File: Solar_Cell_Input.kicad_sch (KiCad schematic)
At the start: 35 parts, among them Q201 BSS138L, Q202 NVTFWS4D9N04XMTAG, Q203 NVTFWS4D9N04XMTAG, U201 BQ24650

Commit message: nearly finnished CORE pcb
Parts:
- renumbered C202 to C201, C204 to C202, C205 to C203, C206 to C204, C207 to C205, C208 to C206, C209 to C207, C210 to C208, C211 to C209, C201 to C210, C203 to C911, R204 to R203, R205 to R204, R206 to R205, R207 to R206, R208 to R207, R209 to R208, R210 to R209, R211 to R210, R212 to R211, R213 to R212, R203 to R913
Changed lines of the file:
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@@
 		(dnp no)
 		(fields_autoplaced yes)
-		(property "Reference" "R211"
+		(property "Reference" "R210"
 			(at 203.2 55.88 90)
 			(effects
@@
 		(dnp no)
 		(fields_autoplaced yes)
-		(property "Reference" "R208"
+		(property "Reference" "R207"
 			(at 139.7 41.9099 0)
 			(effects
@@
 		(on_board yes)
 		(dnp no)
-		(property "Reference" "R210"
+		(property "Reference" "R209"
 			(at 180.594 90.17 0)
 			(effects
@@
 		(on_board yes)
 		(dnp no)
-		(property "Reference" "#PWR0216"
+		(property "Reference" "#PWR0215"
 			(at 213.36 74.93 0)
 			(effects
@@
 		(dnp no)
 		(fields_autoplaced yes)
-		(property "Reference" "#PWR0207"
+		(property "Reference" "#PWR0917"
 			(at 121.92 110.49 0)
 			(effects
@@
 		(on_board yes)
 		(dnp no)
-		(property "Reference" "C207"
+		(property "Reference" "C205"
 			(at 166.878 57.912 90)
 			(effects
@@
 		(on_board yes)
 		(dnp no)
-		(property "Reference" "#PWR0214"
+		(property "Reference" "#PWR0213"
 			(at 189.23 52.07 0)
 			(effects
@@
 		(dnp no)
 		(fields_autoplaced yes)
-		(property "Reference" "R205"
+		(property "Reference" "R204"
 			(at 100.33 78.7399 0)
 			(effects
@@
 		(dnp no)
 		(fields_autoplaced yes)
-		(property "Reference" "R204"
+		(property "Reference" "R203"
 			(at 100.33 66.0399 0)
 			(effects
@@
 		(dnp no)
 		(fields_autoplaced yes)
-		(property "Reference" "#PWR0209"
+		(property "Reference" "#PWR0208"
 			(at 137.16 102.87 0)
 			(effects
@@
 		(on_board yes)
 		(dnp no)
-		(property "Reference" "#PWR0208"
+		(property "Reference" "#PWR0207"
 			(at 123.19 59.69 0)
 			(effects
@@
 		(on_board yes)
 		(dnp no)
-		(property "Reference" "C210"
+		(property "Reference" "C208"
 			(at 208.28 82.5562 0)
 			(effects
@@
 		(on_board yes)
 		(dnp no)
-		(property "Reference" "Q201"
+		(property "Reference" "Q?"
 			(at 91.44 110.49 0)
 			(effects
@@
 				)
 			)
+			(project "EPS"
+				(path "/94201994-47b8-4213-8d1a-05da12b2a7b0/c37f0a0b-f6f4-4c63-8ce8-6ee6766e791f/41c5534f-fcb2-4ec3-adc7-992b7bee1600"
+					(reference "Q?")
+					(unit 1)
+				)
+				(path "/94201994-47b8-4213-8d1a-05da12b2a7b0/c37f0a0b-f6f4-4c63-8ce8-6ee6766e791f/4313468d-8f4f-4bdc-8385-889814f4cee5"
+					(reference "Q?")
+					(unit 1)
+				)
+				(path "/94201994-47b8-4213-8d1a-05da12b2a7b0/c37f0a0b-f6f4-4c63-8ce8-6ee6766e791f/52873e6b-e08e-4161-9ef2-2b4737346b9b"
+					(reference "Q?")
+					(unit 1)
+				)
+				(path "/94201994-47b8-4213-8d1a-05da12b2a7b0/c37f0a0b-f6f4-4c63-8ce8-6ee6766e791f/65753da0-d365-4e1b-a747-1fe94f193180"
+					(reference "Q?")
+					(unit 1)
+				)
+				(path "/94201994-47b8-4213-8d1a-05da12b2a7b0/c37f0a0b-f6f4-4c63-8ce8-6ee6766e791f/6d13a628-cc69-4882-8d71-6117aca3a662"
+					(reference "Q?")
+					(unit 1)
+				)
+				(path "/94201994-47b8-4213-8d1a-05da12b2a7b0/c37f0a0b-f6f4-4c63-8ce8-6ee6766e791f/9d09256a-b1cf-431e-ac15-ed14acab8c88"
+					(reference "Q?")
+					(unit 1)
+				)
+			)
 		)
 	)
@@
 		(dnp no)
 		(fields_autoplaced yes)
-		(property "Reference" "R206"
+		(property "Reference" "R205"
 			(at 107.95 53.3399 0)
 			(effects
@@
 		(on_board yes)
 		(dnp no)
-		(property "Reference" "#PWR0215"
+		(property "Reference" "#PWR0214"
 			(at 208.28 74.93 0)
 			(effects
@@
 		(dnp no)
 		(fields_autoplaced yes)
-		(property "Reference" "R212"
+		(property "Reference" "R211"
 			(at 218.44 82.5499 0)
 			(effects
@@
 		(on_board yes)
 		(dnp no)
-		(property "Reference" "C208"
+		(property "Reference" "C206"
 			(at 191.77 41.9162 0)
 			(effects
@@
 		(on_board yes)
 		(dnp no)
-		(property "Reference" "C209"
+		(property "Reference" "C207"
 			(at 205.74 64.7762 0)
 			(effects
@@
 		(on_board yes)
 		(dnp no)
-		(property "Reference" "#PWR0212"
+		(property "Reference" "#PWR0211"
 			(at 179.07 77.47 0)
 			(effects
@@
 		(on_board yes)
 		(dnp no)
-		(property "Reference" "C204"
+		(property "Reference" "C202"
 			(at 120.65 49.5362 0)
 			(effects
@@
 		(on_board yes)
 		(dnp no)
-		(property "Reference" "C211"
+		(property "Reference" "C209"
 			(at 215.9 64.7762 0)
 			(effects
@@
 		(dnp no)
 		(fields_autoplaced yes)
-		(property "Reference" "#PWR0213"
+		(property "Reference" "#PWR?"
 			(at 173.99 92.71 0)
 			(effects
@@
 				)
 			)
+			(project "EPS"
+				(path "/94201994-47b8-4213-8d1a-05da12b2a7b0/c37f0a0b-f6f4-4c63-8ce8-6ee6766e791f/41c5534f-fcb2-4ec3-adc7-992b7bee1600"
+					(reference "#PWR?")
+					(unit 1)
+				)
+				(path "/94201994-47b8-4213-8d1a-05da12b2a7b0/c37f0a0b-f6f4-4c63-8ce8-6ee6766e791f/4313468d-8f4f-4bdc-8385-889814f4cee5"
+					(reference "#PWR?")
+					(unit 1)
+				)
+				(path "/94201994-47b8-4213-8d1a-05da12b2a7b0/c37f0a0b-f6f4-4c63-8ce8-6ee6766e791f/52873e6b-e08e-4161-9ef2-2b4737346b9b"
+					(reference "#PWR?")
+					(unit 1)
+				)
+				(path "/94201994-47b8-4213-8d1a-05da12b2a7b0/c37f0a0b-f6f4-4c63-8ce8-6ee6766e791f/65753da0-d365-4e1b-a747-1fe94f193180"
+					(reference "#PWR?")
+					(unit 1)
+				)
+				(path "/94201994-47b8-4213-8d1a-05da12b2a7b0/c37f0a0b-f6f4-4c63-8ce8-6ee6766e791f/6d13a628-cc69-4882-8d71-6117aca3a662"
+					(reference "#PWR?")
+					(unit 1)
+				)
+				(path "/94201994-47b8-4213-8d1a-05da12b2a7b0/c37f0a0b-f6f4-4c63-8ce8-6ee6766e791f/9d09256a-b1cf-431e-ac15-ed14acab8c88"
+					(reference "#PWR?")
+					(unit 1)
+				)
+			)
 		)
 	)
@@
 		(on_board yes)
 		(dnp no)
-		(property "Reference" "#PWR0217"
+		(property "Reference" "#PWR0216"
 			(at 215.9 100.33 0)
 			(effects
@@
 		(on_board yes)
 		(dnp no)
-		(property "Reference" "C202"
+		(property "Reference" "C201"
 			(at 113.03 66.0462 0)
 			(effects
@@
 		(dnp no)
 		(fields_autoplaced yes)
-		(property "Reference" "#FLG0201"
+		(property "Reference" "#FLG04701"
 			(at 129.54 45.085 0)
 			(effects
@@
 		(on_board yes)
 		(dnp no)
-		(property "Reference" "C205"
+		(property "Reference" "C203"
 			(at 160.02 72.3962 0)
 			(effects
@@
 		(dnp no)
 		(fields_autoplaced yes)
-		(property "Reference" "#PWR0202"
+		(property "Reference" "#PWR0203"
 			(at 88.9 123.19 0)
 			(effects
@@
 		(on_board yes)
 		(dnp no)
-		(property "Reference" "R209"
+		(property "Reference" "R208"
 			(at 172.212 90.17 0)
 			(effects
@@
 		(dnp no)
 		(fields_autoplaced yes)
-		(property "Reference" "R207"
+		(property "Reference" "R206"
 			(at 107.95 100.3299 0)
 			(effects
@@
 		(on_board yes)
 		(dnp no)
-		(property "Reference" "C203"
+		(property "Reference" "C911"
 			(at 119.38 100.3362 0)
 			(effects
@@
 		(on_board yes)
 		(dnp no)
-		(property "Reference" "#PWR0210"
+		(property "Reference" "#PWR0209"
 			(at 158.75 55.88 0)
 			(effects
@@
 		(dnp no)
 		(fields_autoplaced yes)
-		(property "Reference" "R203"
+		(property "Reference" "R913"
 			(at 91.44 100.3299 0)
 			(effects
@@
 		(on_board yes)
 		(dnp no)
-		(property "Reference" "C201"
+		(property "Reference" "C210"
 			(at 95.25 46.9962 0)
 			(effects
@@
 		(on_board yes)
 		(dnp no)
-		(property "Reference" "#PWR0203"
+		(property "Reference" "#PWR0202"
 			(at 97.79 57.15 0)
 			(effects
@@
 		(dnp no)
 		(fields_autoplaced yes)
-		(property "Reference" "#PWR0211"
+		(property "Reference" "#PWR?"
 			(at 179.07 92.71 0)
 			(effects
@@
 				)
 			)
+			(project "EPS"
+				(path "/94201994-47b8-4213-8d1a-05da12b2a7b0/c37f0a0b-f6f4-4c63-8ce8-6ee6766e791f/41c5534f-fcb2-4ec3-adc7-992b7bee1600"
+					(reference "#PWR?")
+					(unit 1)
+				)
+				(path "/94201994-47b8-4213-8d1a-05da12b2a7b0/c37f0a0b-f6f4-4c63-8ce8-6ee6766e791f/4313468d-8f4f-4bdc-8385-889814f4cee5"
+					(reference "#PWR?")
+					(unit 1)
+				)
+				(path "/94201994-47b8-4213-8d1a-05da12b2a7b0/c37f0a0b-f6f4-4c63-8ce8-6ee6766e791f/52873e6b-e08e-4161-9ef2-2b4737346b9b"
+					(reference "#PWR?")
+					(unit 1)
+				)
+				(path "/94201994-47b8-4213-8d1a-05da12b2a7b0/c37f0a0b-f6f4-4c63-8ce8-6ee6766e791f/65753da0-d365-4e1b-a747-1fe94f193180"
+					(reference "#PWR?")
+					(unit 1)
+				)
+				(path "/94201994-47b8-4213-8d1a-05da12b2a7b0/c37f0a0b-f6f4-4c63-8ce8-6ee6766e791f/6d13a628-cc69-4882-8d71-6117aca3a662"
+					(reference "#PWR?")
+					(unit 1)
+				)
+				(path "/94201994-47b8-4213-8d1a-05da12b2a7b0/c37f0a0b-f6f4-4c63-8ce8-6ee6766e791f/9d09256a-b1cf-431e-ac15-ed14acab8c88"
+					(reference "#PWR?")
+					(unit 1)
+				)
+			)
 		)
 	)
@@
 		(on_board yes)
 		(dnp no)
-		(property "Reference" "C206"
+		(property "Reference" "C204"
 			(at 156.21 45.7262 0)
 			(effects
@@
 		(dnp no)
 		(fields_autoplaced yes)
-		(property "Reference" "R213"
+		(property "Reference" "R212"
 			(at 218.44 90.1699 0)
 			(effects

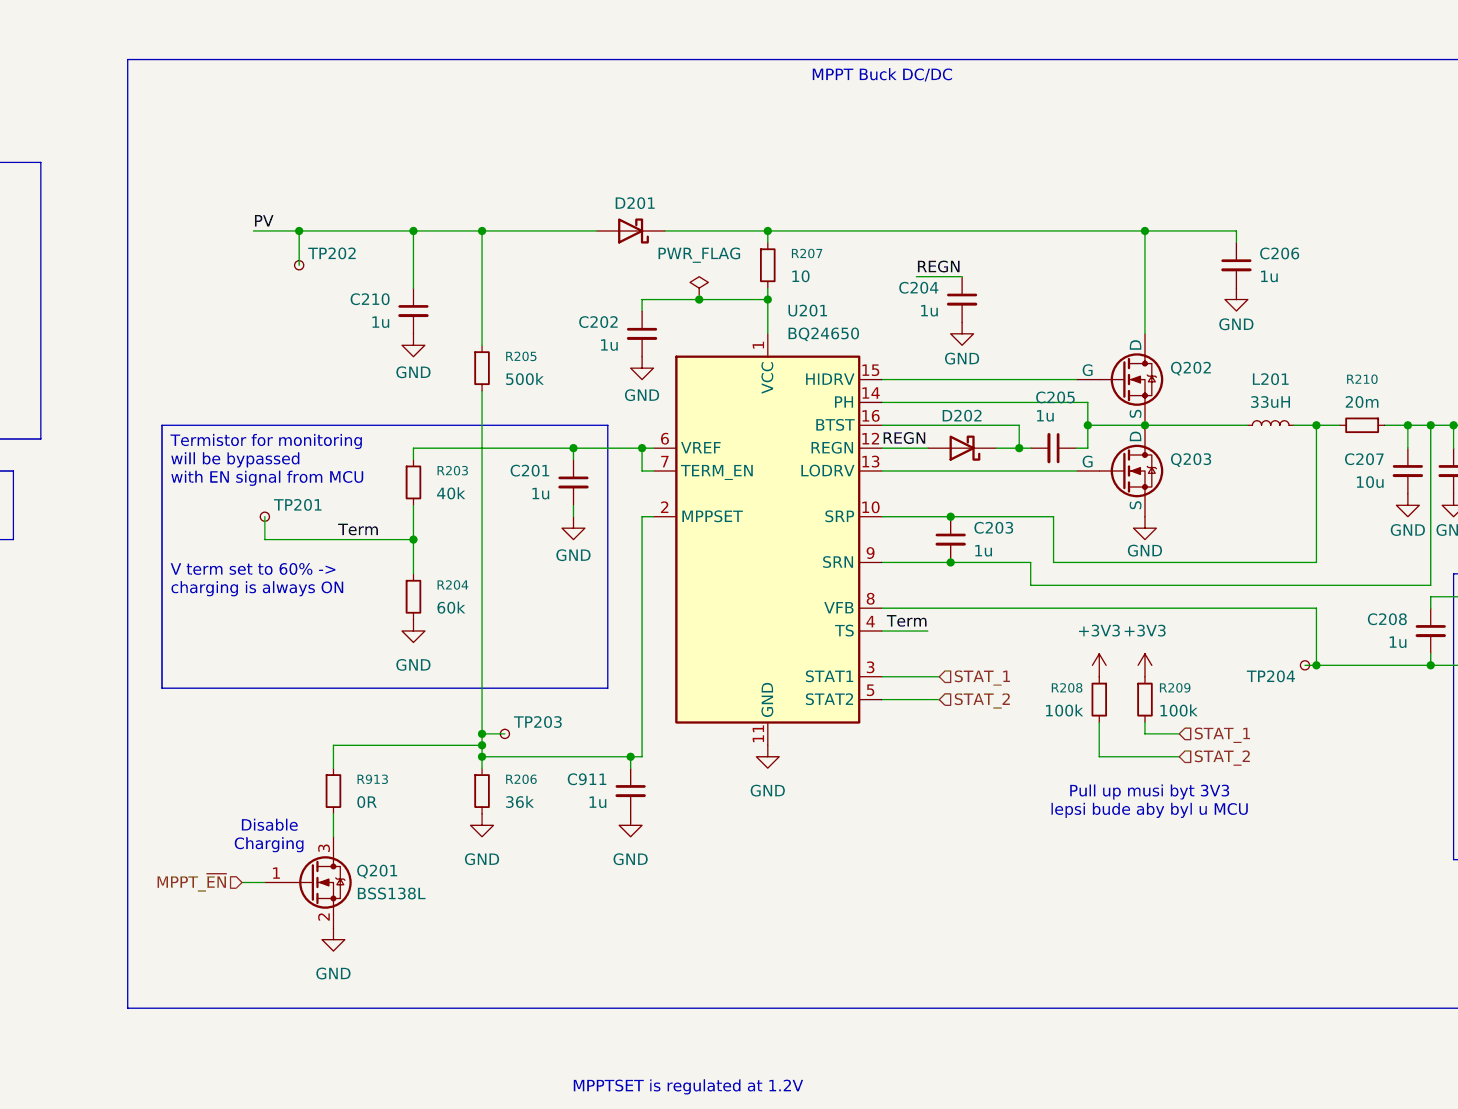
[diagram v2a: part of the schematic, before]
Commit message: pcb progres for all components
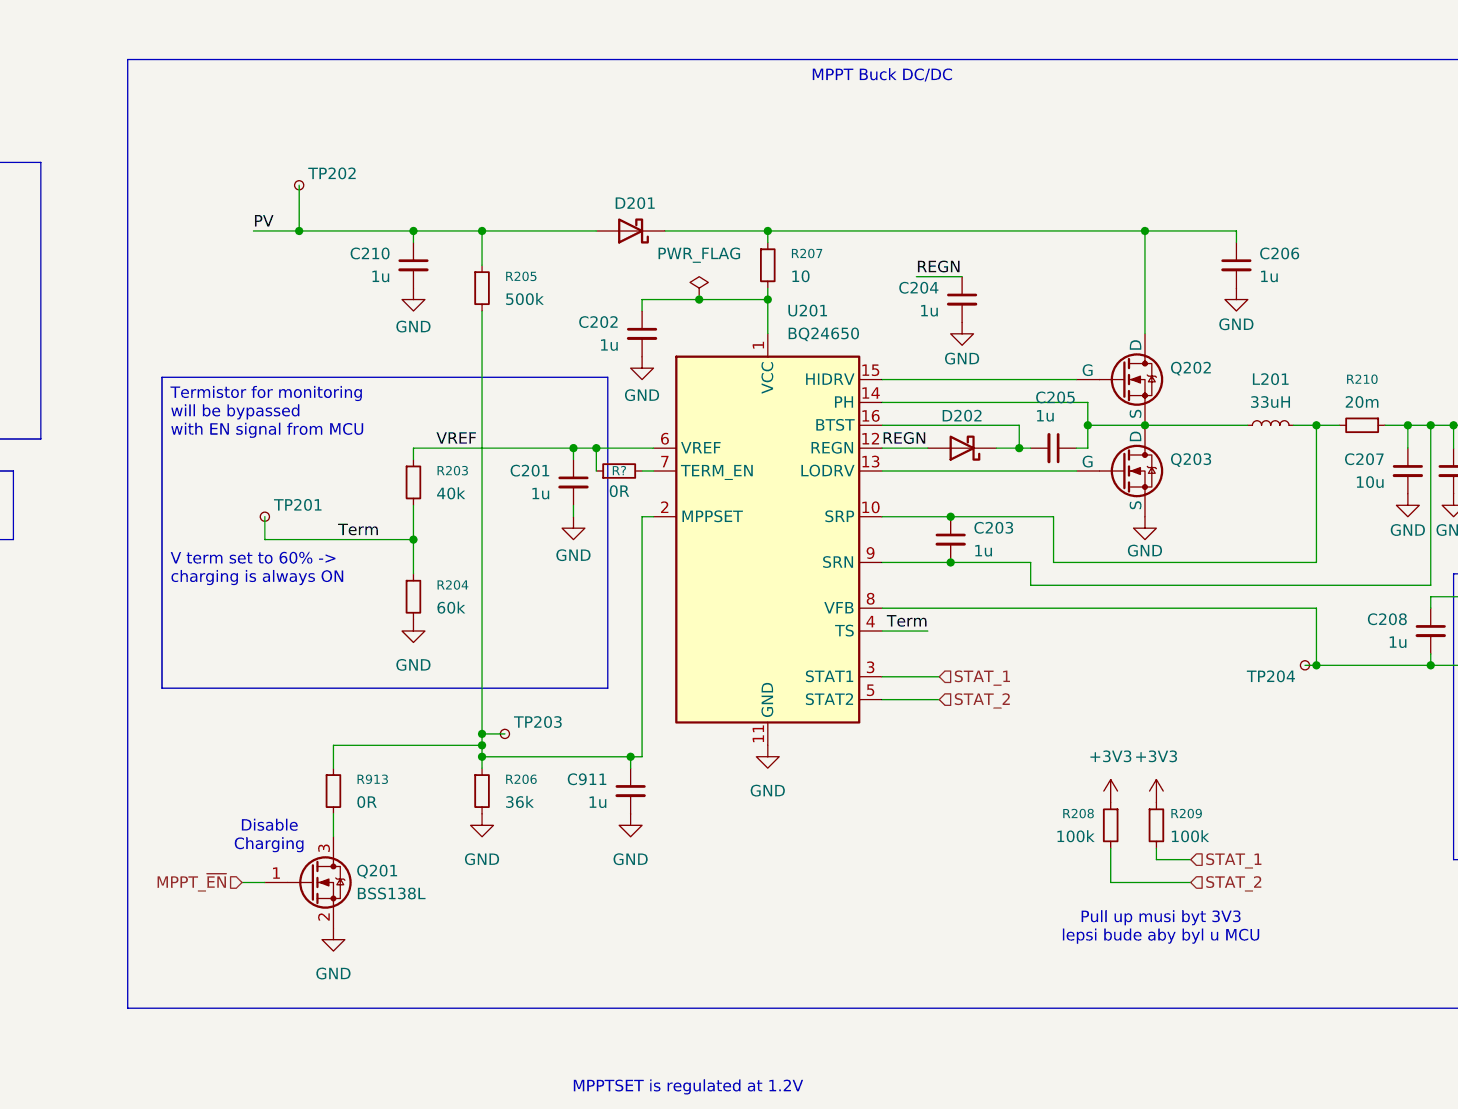
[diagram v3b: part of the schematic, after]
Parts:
- added R?: 0R, Resistor_SMD:R_0603_1608Metric_Pad0.98x0.95mm_HandSolder, symbol Device:R_Small
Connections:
- net VREF: now reaches C201.1, R203.1, U201.6 (VREF)
- net VREF: now also R?.1; no longer U201.7 (TERM_EN)
- new net: R?.2, U201.7 (TERM_EN)
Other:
- moved on the sheet: C210, R205, R208, R209, TP202
